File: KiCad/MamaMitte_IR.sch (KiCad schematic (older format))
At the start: 13 parts, among them Q1 2SC2411K, U4 TC7W04FK

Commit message: Add footprints and assign nets
Assigned and placed footprints, and assigned nets to vias.
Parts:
- C10, C11: footprint (none) -> MamaMitte:C_1210_3225Metric
- C6: footprint (none) -> MamaMitte:C_0402_1005Metric
- C7: footprint (none) -> MamaMitte:C_1206_3216Metric
- Q1: value 2SC2411K -> 2SC4097; footprint (none) -> MamaMitte:SOT-323_SC-70
- R3, R4, R5, R6, R8: footprint (none) -> MamaMitte:R_0402_1005Metric
- U4: footprint (none) -> MamaMitte:SSOP-8_2.3x2mm_P0.5mm
- U5: renamed from U?; footprint (none) -> MamaMitte:Vishay_TFMM5xx0; symbol MamaMitte:TFMM53xx -> MamaMitte-rescue:TFMM53xx-MamaMitte
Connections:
- net GND: no longer R3.2
- net IO1: now also R3.2
- net RX: no longer R3.1
- net at Q1.2 (B), R4.1: now also R3.1
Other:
- note added: "Capacitor Sizes:\n\n1206: C7\n1210: C10, C11\n0402: All others\n"
- moved on the sheet: R3
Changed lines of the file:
@@
 F 0 "U4" H 7050 3700 50  0000 C CNN
 F 1 "TC7W04FK" H 7175 3600 50  0000 C CNN
-F 2 "" H 7450 3425 50  0001 C CNN
+F 2 "MamaMitte:SSOP-8_2.3x2mm_P0.5mm" H 7450 3425 50  0001 C CNN
 F 3 "https://toshiba.semicon-storage.com/info/docget.jsp?did=20206&prodName=TC7W04FU" H 7450 3425 50  0001 C CNN
 	1    7450 3425
@@
 F 0 "U4" H 7050 4425 50  0000 C CNN
 F 1 "TC7W04FK" H 7175 4325 50  0000 C CNN
-F 2 "" H 7450 4150 50  0001 C CNN
+F 2 "MamaMitte:SSOP-8_2.3x2mm_P0.5mm" H 7450 4150 50  0001 C CNN
 F 3 "https://toshiba.semicon-storage.com/info/docget.jsp?did=20206&prodName=TC7W04FU" H 7450 4150 50  0001 C CNN
 	2    7450 4150
@@
 F 0 "C11" H 4590 4021 50  0000 L CNN
 F 1 "C106" H 4590 3930 50  0000 L CNN
-F 2 "" H 4513 3825 50  0001 C CNN
+F 2 "MamaMitte:C_1210_3225Metric" H 4513 3825 50  0001 C CNN
 F 3 "~" H 4475 3975 50  0001 C CNN
 	1    4475 3975
@@
 F 0 "C10" H 5665 5146 50  0000 L CNN
 F 1 "C106" H 5665 5055 50  0000 L CNN
-F 2 "" H 5588 4950 50  0001 C CNN
+F 2 "MamaMitte:C_1210_3225Metric" H 5588 4950 50  0001 C CNN
 F 3 "~" H 5550 5100 50  0001 C CNN
 	1    5550 5100
@@
 P 5850 4125
 F 0 "Q1" H 6040 4171 50  0000 L CNN
-F 1 "2SC2411K" H 6040 4080 50  0000 L CNN
-F 2 "" H 6050 4225 50  0001 C CNN
+F 1 "2SC4097" H 6040 4080 50  0000 L CNN
+F 2 "MamaMitte:SOT-323_SC-70" H 6050 4225 50  0001 C CNN
 F 3 "~" H 5850 4125 50  0001 C CNN
 	1    5850 4125
@@
 $EndComp
 $Comp
-L power:GND #PWR?
+L power:GND #PWR0115
 U 1 1 60AFAA1D
 P 5950 4325
-F 0 "#PWR?" H 5950 4075 50  0001 C CNN
+F 0 "#PWR0115" H 5950 4075 50  0001 C CNN
 F 1 "GND" H 5955 4152 50  0000 C CNN
 F 2 "" H 5950 4325 50  0001 C CNN
@@
 F 0 "R4" V 5400 4125 50  0000 C CNN
 F 1 "R" V 5500 4125 50  0000 C CNN
-F 2 "" V 5430 4125 50  0001 C CNN
+F 2 "MamaMitte:R_0402_1005Metric" V 5430 4125 50  0001 C CNN
 F 3 "~" H 5500 4125 50  0001 C CNN
 	1    5500 4125
@@
 	0    -1   -1   0
 $EndComp
-Text Label 5225 4125 0    50   ~ 0
-TX
-Wire Wire Line
-	5225 4125 5350 4125
 $Comp
 L Device:R R5
@@
 F 0 "R5" H 6025 3475 50  0000 L CNN
 F 1 "R" V 5950 3450 50  0000 L CNN
-F 2 "" V 5880 3475 50  0001 C CNN
+F 2 "MamaMitte:R_0402_1005Metric" V 5880 3475 50  0001 C CNN
 F 3 "~" H 5950 3475 50  0001 C CNN
 	1    5950 3475
@@
 F 0 "R6" H 4550 3575 50  0000 L CNN
 F 1 "R" V 4475 3550 50  0000 L CNN
-F 2 "" V 4405 3575 50  0001 C CNN
+F 2 "MamaMitte:R_0402_1005Metric" V 4405 3575 50  0001 C CNN
 F 3 "~" H 4475 3575 50  0001 C CNN
 	1    4475 3575
@@
 F 0 "C6" H 6090 5146 50  0000 L CNN
 F 1 "C104" H 6090 5055 50  0000 L CNN
-F 2 "" H 6013 4950 50  0001 C CNN
+F 2 "MamaMitte:C_0402_1005Metric" H 6013 4950 50  0001 C CNN
 F 3 "~" H 5975 5100 50  0001 C CNN
 	1    5975 5100
@@
 $EndComp
 $Comp
-L power:+3.3V #PWR?
+L power:+3.3V #PWR0116
 U 1 1 60B51F3A
 P 5950 3325
-F 0 "#PWR?" H 5950 3175 50  0001 C CNN
+F 0 "#PWR0116" H 5950 3175 50  0001 C CNN
 F 1 "+3.3V" H 5965 3498 50  0000 C CNN
 F 2 "" H 5950 3325 50  0001 C CNN
@@
 $EndComp
 $Comp
-L power:GND #PWR?
+L power:GND #PWR0117
 U 1 1 60B69FD5
 P 5550 5250
-F 0 "#PWR?" H 5550 5000 50  0001 C CNN
+F 0 "#PWR0117" H 5550 5000 50  0001 C CNN
 F 1 "GND" H 5555 5077 50  0000 C CNN
 F 2 "" H 5550 5250 50  0001 C CNN
@@
 Transmitter
 $Comp
-L power:+3.3V #PWR?
+L power:+3.3V #PWR0118
 U 1 1 60B9628A
 P 5550 4950
-F 0 "#PWR?" H 5550 4800 50  0001 C CNN
+F 0 "#PWR0118" H 5550 4800 50  0001 C CNN
 F 1 "+3.3V" H 5565 5123 50  0000 C CNN
 F 2 "" H 5550 4950 50  0001 C CNN
@@
 F 0 "C7" H 4590 2621 50  0000 L CNN
 F 1 "C" H 4590 2530 50  0000 L CNN
-F 2 "" H 4513 2425 50  0001 C CNN
+F 2 "MamaMitte:C_1206_3216Metric" H 4513 2425 50  0001 C CNN
 F 3 "~" H 4475 2575 50  0001 C CNN
 	1    4475 2575
@@
 $EndComp
 $Comp
-L power:GND #PWR?
+L power:GND #PWR0119
 U 1 1 60BC38E8
 P 4475 4225
-F 0 "#PWR?" H 4475 3975 50  0001 C CNN
+F 0 "#PWR0119" H 4475 3975 50  0001 C CNN
 F 1 "GND" H 4480 4052 50  0000 C CNN
 F 2 "" H 4475 4225 50  0001 C CNN
@@
 $EndComp
 $Comp
-L power:GND #PWR?
+L power:GND #PWR0120
 U 1 1 60BE4344
 P 4475 2725
-F 0 "#PWR?" H 4475 2475 50  0001 C CNN
+F 0 "#PWR0120" H 4475 2475 50  0001 C CNN
 F 1 "GND" H 4480 2552 50  0000 C CNN
 F 2 "" H 4475 2725 50  0001 C CNN
@@
 $EndComp
 $Comp
-L power:+3.3V #PWR?
+L power:+3.3V #PWR0121
 U 1 1 60C35ED0
 P 7500 3375
-F 0 "#PWR?" H 7500 3225 50  0001 C CNN
+F 0 "#PWR0121" H 7500 3225 50  0001 C CNN
 F 1 "+3.3V" H 7515 3548 50  0000 C CNN
 F 2 "" H 7500 3375 50  0001 C CNN
@@
 Connection ~ 7500 3600
 $Comp
-L power:GND #PWR?
+L power:GND #PWR0122
 U 1 1 60AB1460
 P 7500 3600
-F 0 "#PWR?" H 7500 3350 50  0001 C CNN
+F 0 "#PWR0122" H 7500 3350 50  0001 C CNN
 F 1 "GND" H 7505 3427 50  0000 C CNN
 F 2 "" H 7500 3600 50  0001 C CNN
@@
 $EndComp
 $Comp
-L power:+3.3V #PWR?
+L power:+3.3V #PWR0123
 U 1 1 60C45B71
 P 7500 4100
-F 0 "#PWR?" H 7500 3950 50  0001 C CNN
+F 0 "#PWR0123" H 7500 3950 50  0001 C CNN
 F 1 "+3.3V" H 7515 4273 50  0000 C CNN
 F 2 "" H 7500 4100 50  0001 C CNN
@@
 $EndComp
 $Comp
-L power:+3.3V #PWR?
+L power:+3.3V #PWR0124
 U 1 1 60C5667A
 P 7500 4975
-F 0 "#PWR?" H 7500 4825 50  0001 C CNN
+F 0 "#PWR0124" H 7500 4825 50  0001 C CNN
 F 1 "+3.3V" H 7515 5148 50  0000 C CNN
 F 2 "" H 7500 4975 50  0001 C CNN
@@
 F 0 "U4" H 7050 5300 50  0000 C CNN
 F 1 "TC7W04FK" H 7175 5200 50  0000 C CNN
-F 2 "" H 7450 5025 50  0001 C CNN
+F 2 "MamaMitte:SSOP-8_2.3x2mm_P0.5mm" H 7450 5025 50  0001 C CNN
 F 3 "https://toshiba.semicon-storage.com/info/docget.jsp?did=20206&prodName=TC7W04FU" H 7450 5025 50  0001 C CNN
 	3    7450 5025
@@
 	7500 4450 7500 4200
 $Comp
-L power:GND #PWR?
+L power:GND #PWR0125
 U 1 1 60C4F78A
 P 7500 4450
-F 0 "#PWR?" H 7500 4200 50  0001 C CNN
+F 0 "#PWR0125" H 7500 4200 50  0001 C CNN
 F 1 "GND" H 7505 4277 50  0000 C CNN
 F 2 "" H 7500 4450 50  0001 C CNN
@@
 F 0 "R8" H 7150 4300 50  0000 L CNN
 F 1 "R" V 7075 4275 50  0000 L CNN
-F 2 "" V 7005 4300 50  0001 C CNN
+F 2 "MamaMitte:R_0402_1005Metric" V 7005 4300 50  0001 C CNN
 F 3 "~" H 7075 4300 50  0001 C CNN
 	1    7075 4300
@@
 $EndComp
 $Comp
-L power:GND #PWR?
+L power:GND #PWR0126
 U 1 1 60C889E2
-P 7500 5325
-F 0 "#PWR?" H 7500 5075 50  0001 C CNN
-F 1 "GND" H 7505 5152 50  0000 C CNN
-F 2 "" H 7500 5325 50  0001 C CNN
-F 3 "" H 7500 5325 50  0001 C CNN
-	1    7500 5325
-	1    0    0    -1
-$EndComp
-Wire Wire Line
-	7500 5325 7500 5075
-Connection ~ 7500 5325
+P 7500 5075
+F 0 "#PWR0126" H 7500 4825 50  0001 C CNN
+F 1 "GND" H 7505 4902 50  0000 C CNN
+F 2 "" H 7500 5075 50  0001 C CNN
+F 3 "" H 7500 5075 50  0001 C CNN
+	1    7500 5075
+	1    0    0    -1
+$EndComp
 Wire Notes Line
 	8000 3025 6725 3025
@@
 Wire Notes Line
 	6725 5625 8000 5625
-Wire Wire Line
-	7150 5325 7500 5325
-$Comp
-L Device:R R3
-U 1 1 60BF36E0
-P 7150 5175
-F 0 "R3" H 7225 5125 50  0000 L CNN
-F 1 "R" V 7150 5150 50  0000 L CNN
-F 2 "" V 7080 5175 50  0001 C CNN
-F 3 "~" H 7150 5175 50  0001 C CNN
-	1    7150 5175
-	1    0    0    -1
-$EndComp
 Text GLabel 7700 5025 2    50   Input ~ 0
 IO1
 $Comp
-L MamaMitte:TFMM53xx U?
+L MamaMitte-rescue:TFMM53xx-MamaMitte U5
 U 1 1 60CC3C52
 P 3750 3975
-F 0 "U?" H 3738 4400 50  0000 C CNN
+AR Path="/60CC3C52" Ref="U5"  Part="1"
+AR Path="/6088E26C/60CC3C52" Ref="U5"  Part="1"
+F 0 "U5" H 3738 4400 50  0000 C CNN
 F 1 "TFMM53xx" H 3738 4309 50  0000 C CNN
-F 2 "" H 3700 3600 50  0001 C CNN
+F 2 "MamaMitte:Vishay_TFMM5xx0" H 3700 3600 50  0001 C CNN
 F 3 "" H 4400 4275 50  0001 C CNN
 	1    3750 3975
@@
 RX
 $Comp
-L power:+3.3V #PWR?
+L power:+3.3V #PWR0127
 U 1 1 60CD28B0
 P 4475 3425
-F 0 "#PWR?" H 4475 3275 50  0001 C CNN
+F 0 "#PWR0127" H 4475 3275 50  0001 C CNN
 F 1 "+3.3V" H 4490 3598 50  0000 C CNN
 F 2 "" H 4475 3425 50  0001 C CNN
@@
 Text Notes 3125 3000 0    50   ~ 0
 Receiver
-Connection ~ 7150 5025
 Text Notes 3175 3300 0    50   ~ 0
 Part unknown.\nClosest: TFMM53xx series.\nIncorrect pinout and params.
+$Comp
+L Device:R R3
+U 1 1 60BF36E0
+P 5500 4300
+F 0 "R3" V 5600 4250 50  0000 L CNN
+F 1 "R" V 5500 4275 50  0000 L CNN
+F 2 "MamaMitte:R_0402_1005Metric" V 5430 4300 50  0001 C CNN
+F 3 "~" H 5500 4300 50  0001 C CNN
+	1    5500 4300
+	0    1    1    0
+$EndComp
+Wire Wire Line
+	5225 4125 5350 4125
+Text Label 5225 4125 0    50   ~ 0
+TX
+Text GLabel 5350 4300 0    50   Input ~ 0
+IO1
+Wire Wire Line
+	5650 4300 5650 4125
+Connection ~ 5650 4125
+Text Notes 800  7675 0    100  ~ 0
+Capacitor Sizes:\n\n1206: C7\n1210: C10, C11\n0402: All others\n
 $EndSCHEMATC

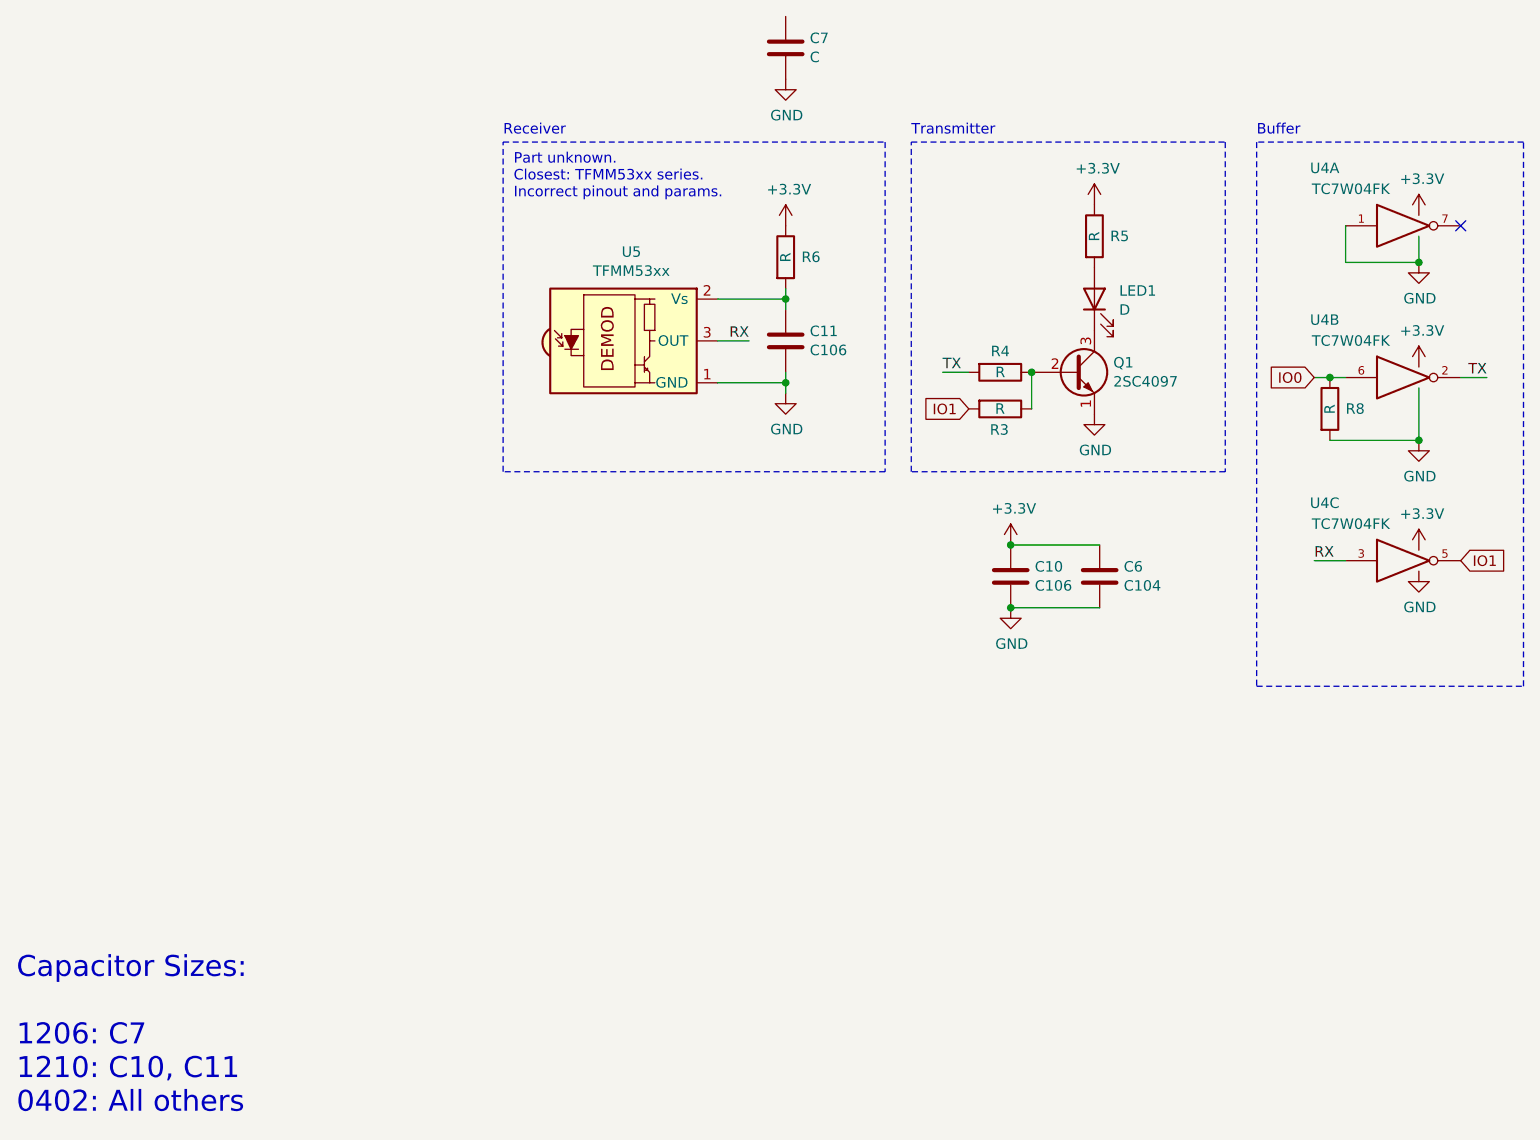
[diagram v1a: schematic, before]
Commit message: Update schematic
Change power source for RTC pull-ups, and restructure IR block.
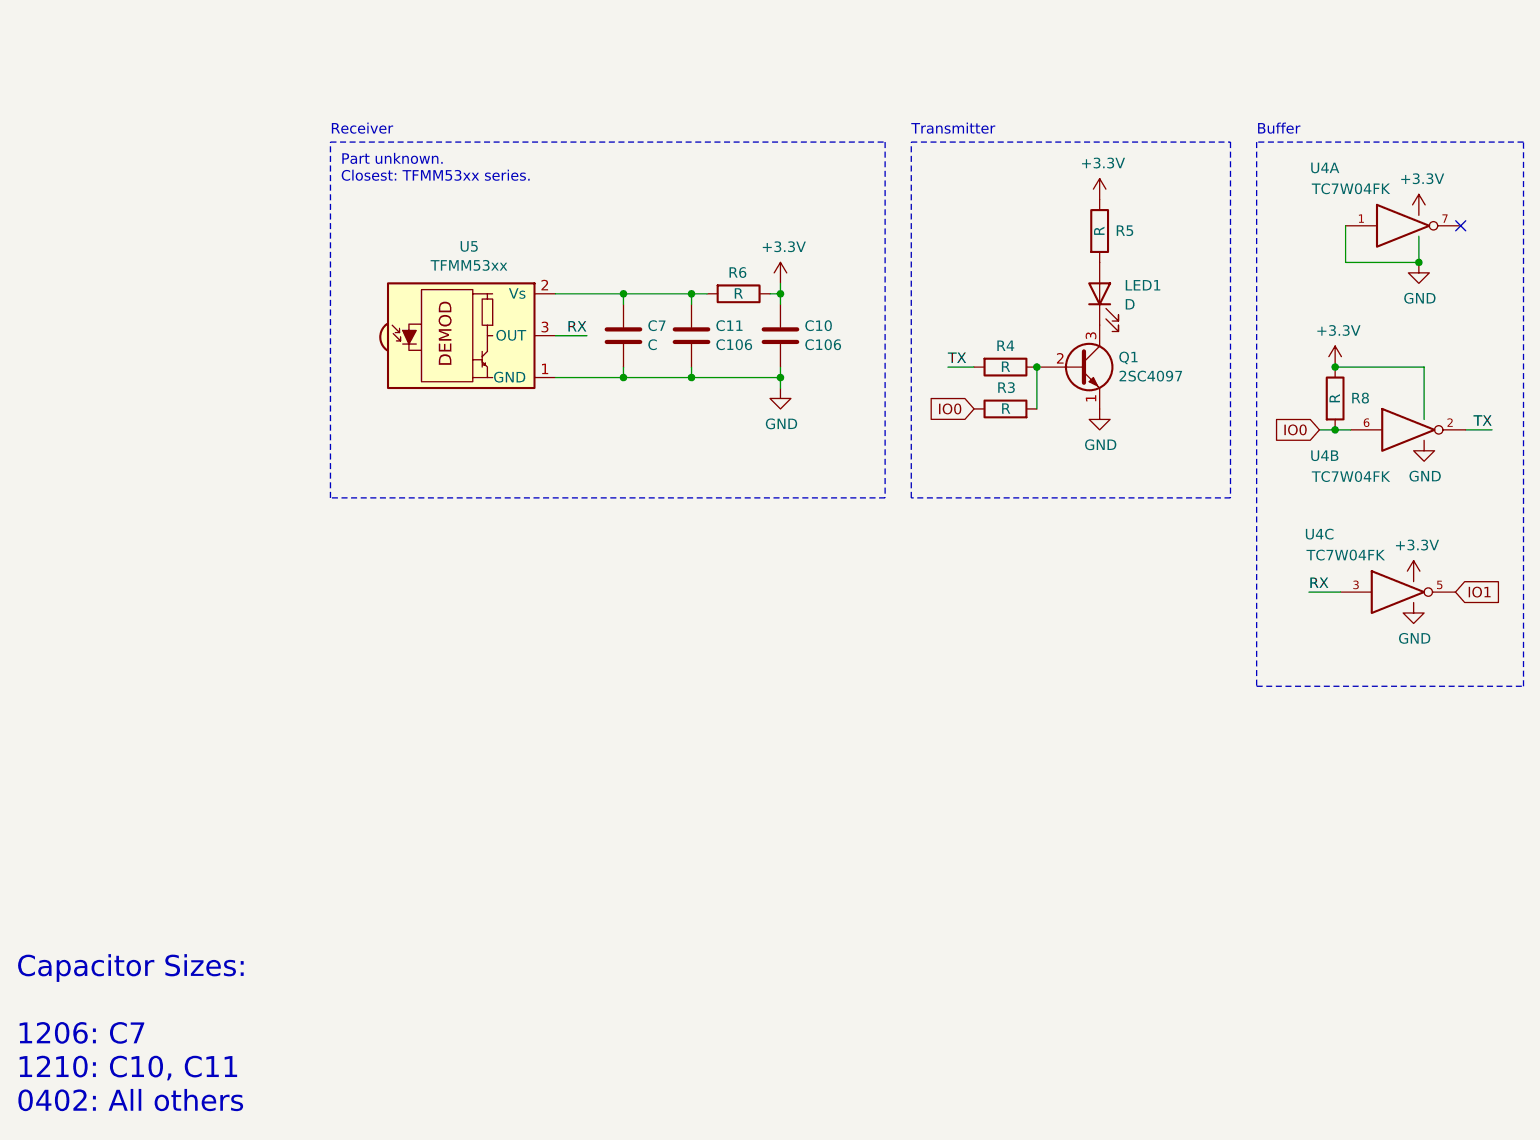
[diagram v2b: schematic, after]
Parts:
- removed C6: C104, MamaMitte:C_0402_1005Metric, symbol Device:C
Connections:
- net +3V3: now also R8.1
- net GND: no longer R8.2
- net IO0: now also R3.1, R8.2; no longer R8.1
- net IO1: no longer R3.2
- net at C11.1, R6.2, U5.2 (Vs): now also C7.1
- net at Q1.2 (B), R4.1: now also R3.2; no longer R3.1
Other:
- note added: "Part unknown.\nClosest: TFMM53xx series."
- note removed: "Part unknown.\nClosest: TFMM53xx series.\nIncorrect pinout and params."
- moved on the sheet: C10, C11, C7, LED1, Q1, R3, R4, R5, R6, R8, U4B, U4C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
